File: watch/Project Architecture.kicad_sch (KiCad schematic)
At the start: 0 parts

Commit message: Add speaker
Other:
- sheet Extension ports: added none; removed SP_{N}, SP_{P}
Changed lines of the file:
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@@
-			)
-		)
-		(pin "SP_{N}" output
-			(at 237.49 185.42 180)
-			(effects
-				(font
-					(size 1.27 1.27)
-				)
-				(justify left)
-			)
-		)
-		(pin "SP_{P}" output
-			(at 237.49 182.88 180)
-			(effects
-				(font
-					(size 1.27 1.27)
-				)
-				(justify left)
 			)
 		)

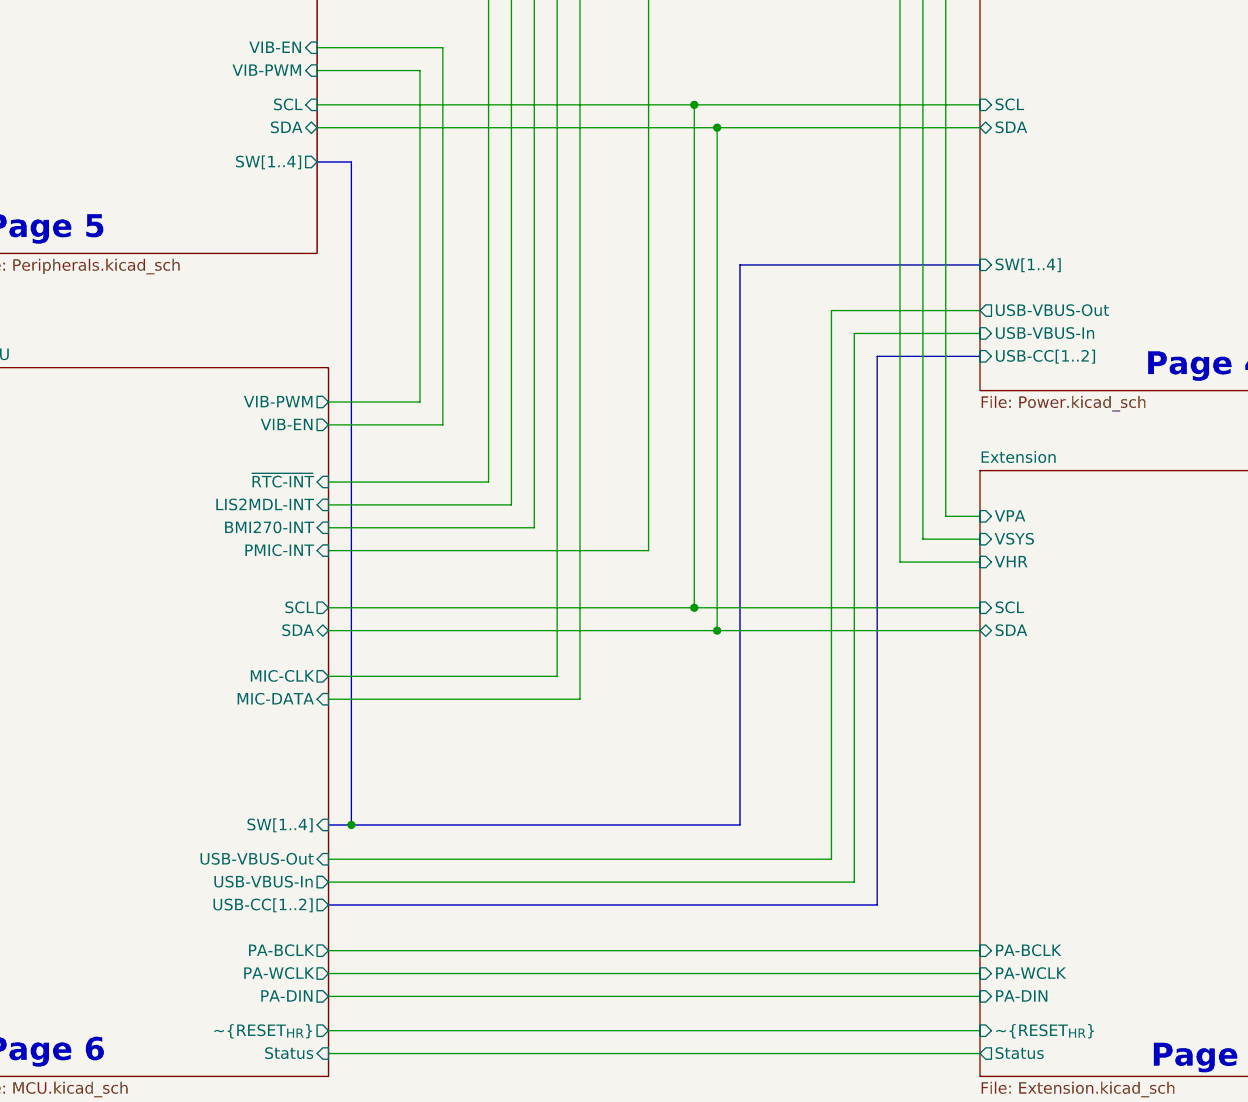
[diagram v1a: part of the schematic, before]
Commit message: Fix wrong Extension footprint
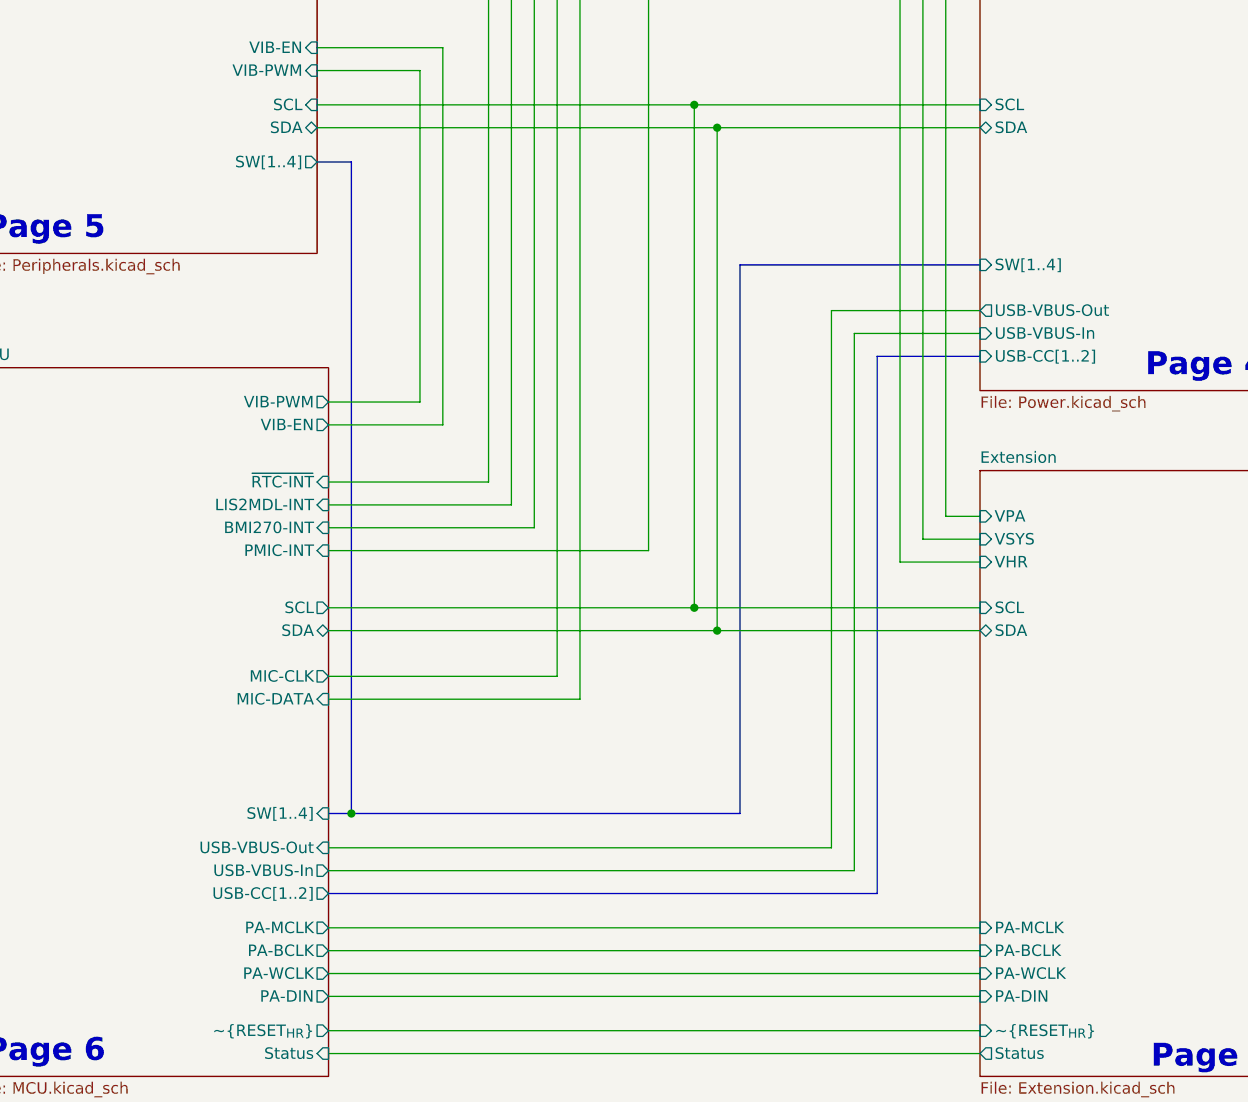
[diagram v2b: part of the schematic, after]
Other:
- sheet Extension ports: added PA-MCLK; removed none
- sheet MCU ports: added PA-MCLK; removed none
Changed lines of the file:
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@@
 	)
 	(junction
-		(at 167.64 175.26)
+		(at 167.64 173.99)
 		(diameter 0)
 		(color 0 0 0 0)
@@
 	(bus
 		(pts
-			(xy 167.64 101.6) (xy 167.64 175.26)
+			(xy 167.64 101.6) (xy 167.64 173.99)
 		)
 		(stroke
@@
 	(bus
 		(pts
-			(xy 165.1 184.15) (xy 226.06 184.15)
+			(xy 165.1 182.88) (xy 226.06 182.88)
 		)
 		(stroke
@@
 	(wire
 		(pts
-			(xy 220.98 179.07) (xy 165.1 179.07)
+			(xy 220.98 177.8) (xy 165.1 177.8)
 		)
 		(stroke
@@
 	(wire
 		(pts
-			(xy 220.98 118.11) (xy 220.98 179.07)
+			(xy 220.98 118.11) (xy 220.98 177.8)
 		)
 		(stroke
@@
 	(bus
 		(pts
-			(xy 210.82 175.26) (xy 167.64 175.26)
+			(xy 210.82 173.99) (xy 167.64 173.99)
 		)
 		(stroke
@@
 	(bus
 		(pts
-			(xy 210.82 113.03) (xy 210.82 175.26)
+			(xy 210.82 113.03) (xy 210.82 173.99)
 		)
 		(stroke
@@
 	(wire
 		(pts
-			(xy 223.52 120.65) (xy 223.52 181.61)
+			(xy 223.52 120.65) (xy 223.52 180.34)
 		)
 		(stroke
@@
 	(bus
 		(pts
-			(xy 226.06 123.19) (xy 226.06 184.15)
+			(xy 226.06 123.19) (xy 226.06 182.88)
 		)
 		(stroke
@@
 	(bus
 		(pts
-			(xy 167.64 175.26) (xy 165.1 175.26)
+			(xy 167.64 173.99) (xy 165.1 173.99)
 		)
 		(stroke
@@
 	(wire
 		(pts
-			(xy 165.1 181.61) (xy 223.52 181.61)
+			(xy 165.1 180.34) (xy 223.52 180.34)
+		)
+		(stroke
+			(width 0)
+			(type default)
+		)
+	)
+	(wire
+		(pts
+			(xy 165.1 186.69) (xy 237.49 186.69)
 		)
 		(stroke
@@
 		)
 		(pin "USB-VBUS-In" output
-			(at 165.1 181.61 0)
+			(at 165.1 180.34 0)
 			(effects
 				(font
@@
 		)
 		(pin "USB-CC[1..2]" output
-			(at 165.1 184.15 0)
+			(at 165.1 182.88 0)
 			(effects
 				(font
@@
 		)
 		(pin "USB-VBUS-Out" input
-			(at 165.1 179.07 0)
+			(at 165.1 177.8 0)
 			(effects
 				(font
@@
 		)
 		(pin "SW[1..4]" input
-			(at 165.1 175.26 0)
+			(at 165.1 173.99 0)
 			(effects
 				(font
@@
 		(pin "PA-BCLK" output
 			(at 165.1 189.23 0)
+			(effects
+				(font
+					(size 1.27 1.27)
+				)
+				(justify right)
+			)
+		)
+		(pin "PA-MCLK" output
+			(at 165.1 186.69 0)
 			(effects
 				(font
@@
 			(effects
 				(font
+					(size 1.27 1.27)
+				)
+				(justify left)
+			)
+		)
+		(pin "PA-MCLK" input
+			(at 237.49 186.69 180)
+			(effects
+				(font
